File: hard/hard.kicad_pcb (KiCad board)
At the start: 2 copper layers, 156.2 x 97.2 mm, 72 parts, among them J1 USB_C_Receptacle_USB2.0, J2 RJ45_LED_Shielded, SW1 SW_RST, SW10 KEY_Q, SW11 KEY_A, SW12 KEY_OPTION, SW13 KEY_2, SW14 KEY_Z, SW15 KEY_W, SW16 KEY_S, SW17 KEY_COMMAND, SW18 KEY_3, SW19 KEY_X, SW2 SW_BOOT0, SW20 KEY_E, SW21 KEY_D, SW22 KEY_4, SW23 KEY_C, SW24 KEY_R, SW25 KEY_F, SW26 KEY_5, SW27 KEY_SPACE, SW28 KEY_V, SW29 KEY_T, SW3 KEY_CAPSLOCK, SW30 KEY_G, SW31 KEY_6, SW32 KEY_B, SW4 KEY_LSHIFT, SW5 KEY_LFN, SW6 KEY_TAB, SW7 KEY_ESCAPE, SW8 KEY_CONTROL, SW9 KEY_1, U1 LTC2852xMS, U2 USBLC6-2SC6, U3 MIC5504-3.3YM5, U4 STLinkV3, U5 STM32L412RBTx, Y1 8MHz

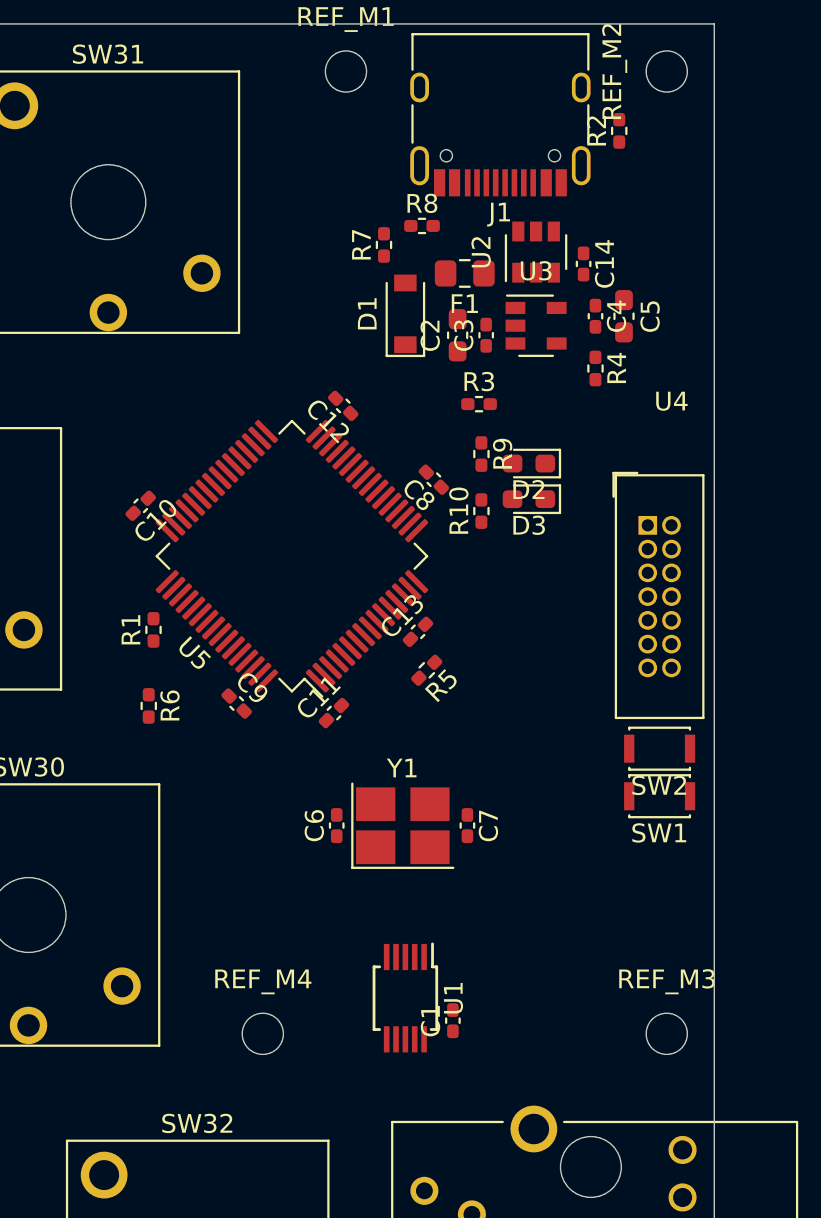
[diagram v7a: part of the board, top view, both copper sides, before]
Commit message: THVD1451D -> THVD1452
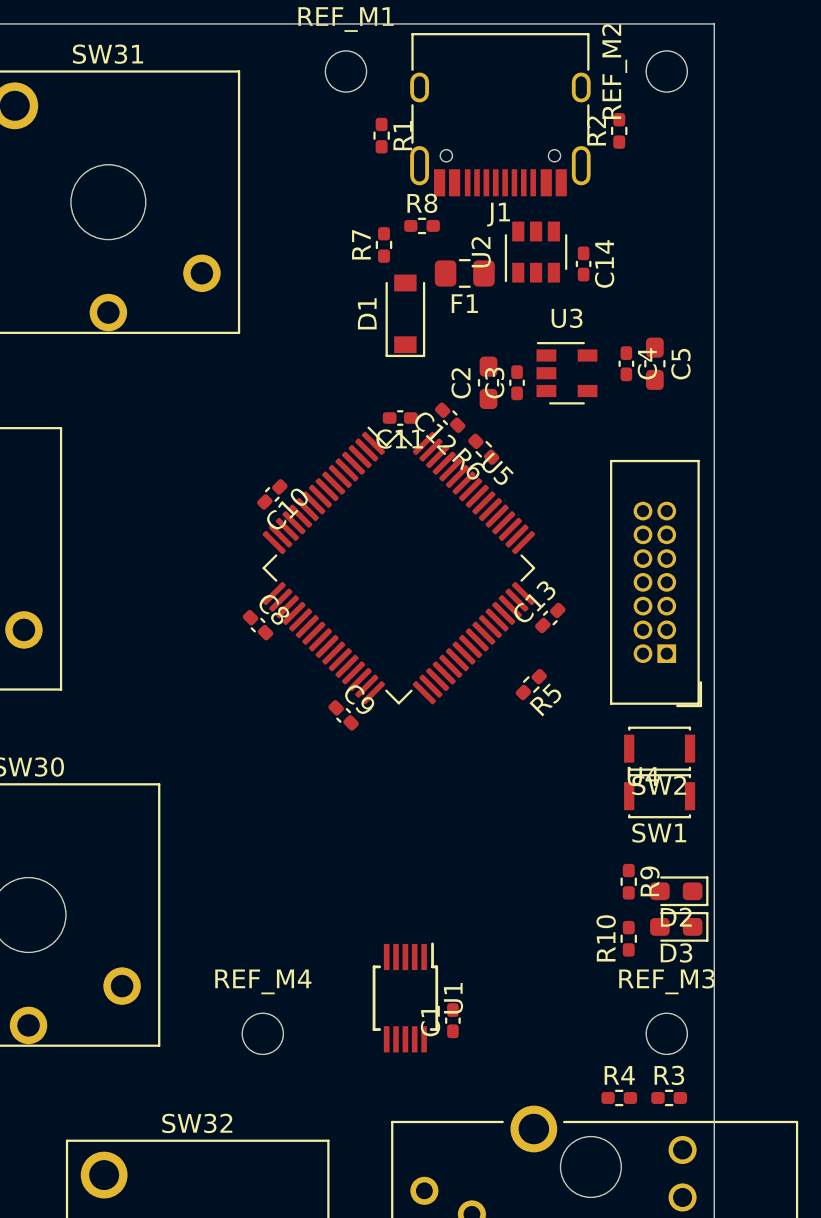
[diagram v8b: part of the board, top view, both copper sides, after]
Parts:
- removed C6, C7: 10pF, Capacitor_SMD:C_0402_1005Metric_Pad0.74x0.62mm_HandSolder
- removed Y1: 8MHz, Crystal:Crystal_SMD_3225-4Pin_3.2x2.5mm_HandSoldering
- moved R4 39.0 mm to (230.5, 123.4), turned to 0 degrees
- moved R3 38.5 mm to (233.2, 123.4)
- moved R1 29.1 mm to (217.8, 72.0), turned to 270 degrees
- moved D2 24.2 mm to (233.6, 112.4)
- moved D3 24.2 mm to (233.6, 114.3)
- moved R10 24.2 mm to (231.0, 114.9)
- moved R9 24.2 mm to (231.0, 111.9)
- moved R6 22.6 mm to (223.3, 88.8), turned to 135 degrees
- moved C11 16.2 mm to (218.8, 87.1), turned to 180 degrees
- moved C8 12.2 mm to (211.2, 98.2), turned to 315 degrees
- moved C13 7.11 mm to (226.8, 97.8)
- moved C10 7.06 mm to (212.0, 91.2)
- moved U4 6.93 mm to (233.0, 99.7), turned to 180 degrees
- moved C12 5.75 mm to (221.5, 87.1)
- moved C9 5.75 mm to (215.8, 103.0)
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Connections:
- J1 pad A8: Net-(J1-PadA8) -> (no net)
- J1 pad B8: Net-(J1-PadB8) -> (no net)
- U3 pad 4: Net-(U3-Pad4) -> (no net)
- U4 pad 1: Net-(U4-Pad1) -> (no net)
- U4 pad 2: Net-(U4-Pad2) -> (no net)
- U5 pad 14: Net-(U5-Pad14) -> (no net)
- U5 pad 15: Net-(U5-Pad15) -> (no net)
- U5 pad 30: Net-(U5-Pad30) -> (no net)
- U5 pad 4: Net-(U5-Pad4) -> (no net)
- U5 pad 5: /XTAL_A -> (no net)
- U5 pad 6: /XTAL_B -> (no net)
- U5 pad 61: Net-(U5-Pad61) -> (no net)
- U5 pad 62: Net-(U5-Pad62) -> (no net)
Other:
- net class Default: clearance 0.2 -> 0.127; trace_width 0.2 -> 0.127
- rule trace_clearance: 0.2 -> 0.127
- rule trace_min: 0.2 -> 0.127
- rule via_min_drill: 0.3 -> 0.2
